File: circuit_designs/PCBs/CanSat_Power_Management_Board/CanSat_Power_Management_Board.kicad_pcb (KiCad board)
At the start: 4 copper layers, 95 x 95 mm, 62 parts, among them J1 MCU Switch (7.4V), J2 7.4V Battery, J3 Sensor Board, J4 Booster Switch (3.7V), J5 3.7V Battery, Q1 BS170, Q2 BSS84, U1 LM2596T-ADJ, U3 NE555P

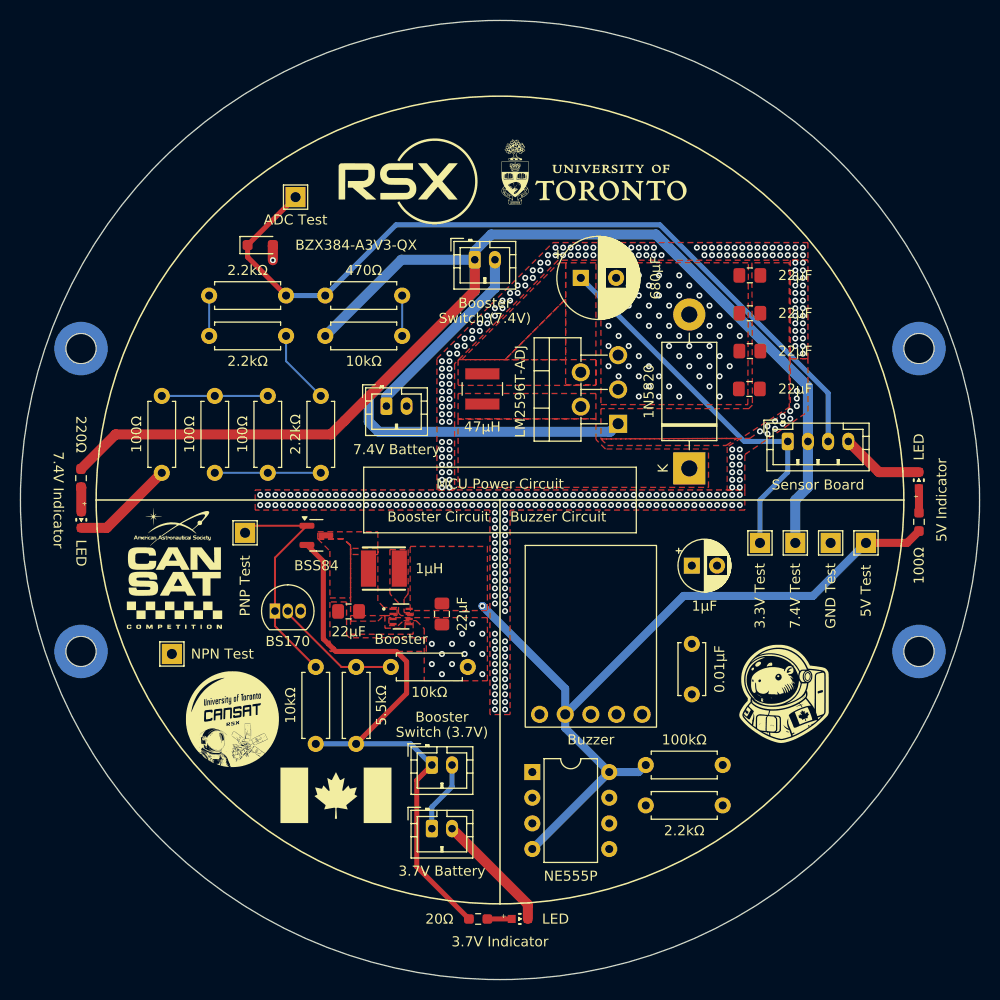
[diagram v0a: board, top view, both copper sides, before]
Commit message: fixed stiching vias - added new logo - fixed some other vias with kc
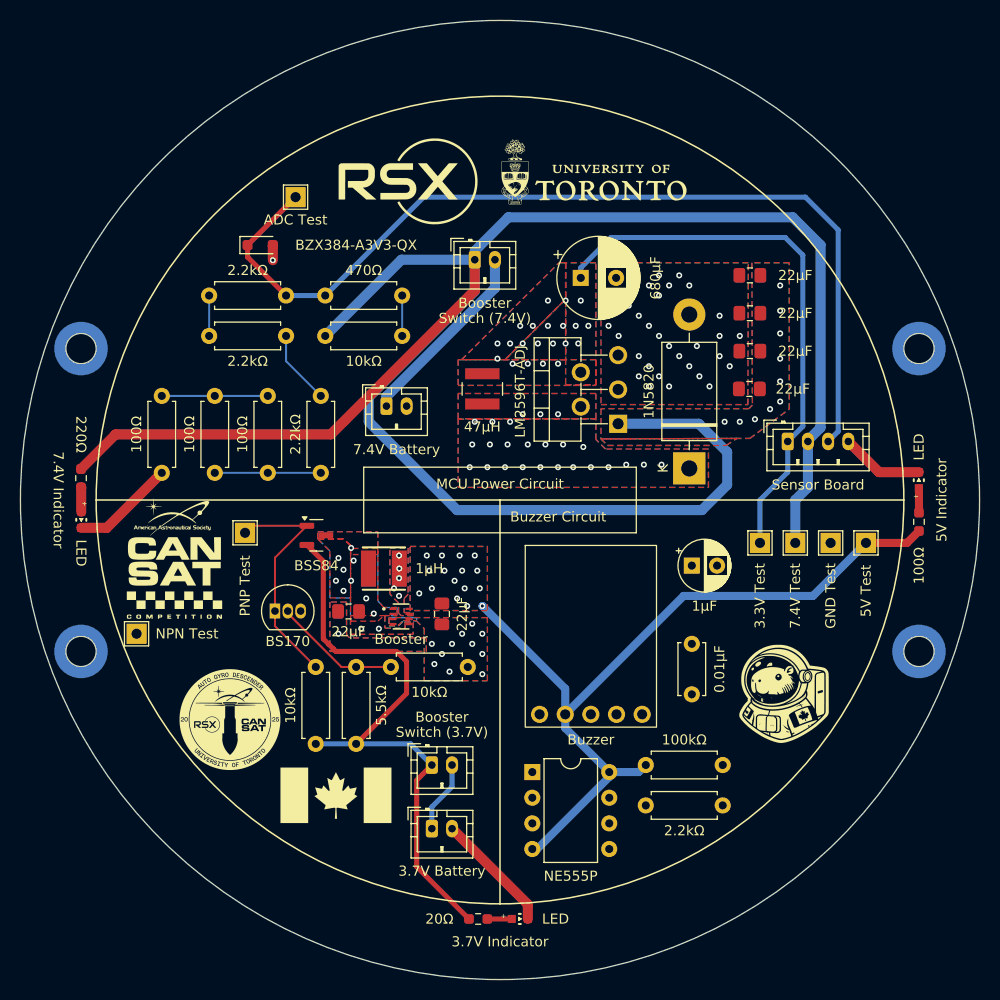
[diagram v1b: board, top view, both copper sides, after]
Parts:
- removed the G*** at (123.5, 121.8)
- added G***: LOGO, Graphics:logo, F.Cu at (123.2, 121.8)
- added G***: LOGO, Graphics:logo_x2, B.Cu at (120.8, 123.0)
- moved TP5 4.03 mm to (114.0, 113.2)
- moved G*** 1.00 mm to (117.8, 105.8)
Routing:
- net 7.4V: track 170.0 -> 211.3 mm, vias 0 -> 10
- net 3.3V: track 38.4 -> 55.2 mm, vias 0 -> 21
- net ADC: track 81.6 -> 94.7 mm
- net /5V: track 78.9 -> 79.2 mm, vias 1 -> 16
- net GND: vias 413 -> 42
- net /VIN: vias 0 -> 11
- net /SW: vias 0 -> 5
- net /OUT: vias 0 -> 25
- added copper zone on B.Cu, net /5V
- added copper zone on B.Cu, net /OUT
- added copper zone on B.Cu, net /SW
- added copper zone on B.Cu, net /VIN
- added copper zone on B.Cu, net 3.3V
- added copper zone on B.Cu, net 7.4V
- added copper zone on B.Cu, net GND
- added copper zone on In2.Cu, net GND
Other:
- board text removed: "Booster Circuit"

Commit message: fixed errors and exposed copper for thermal pads
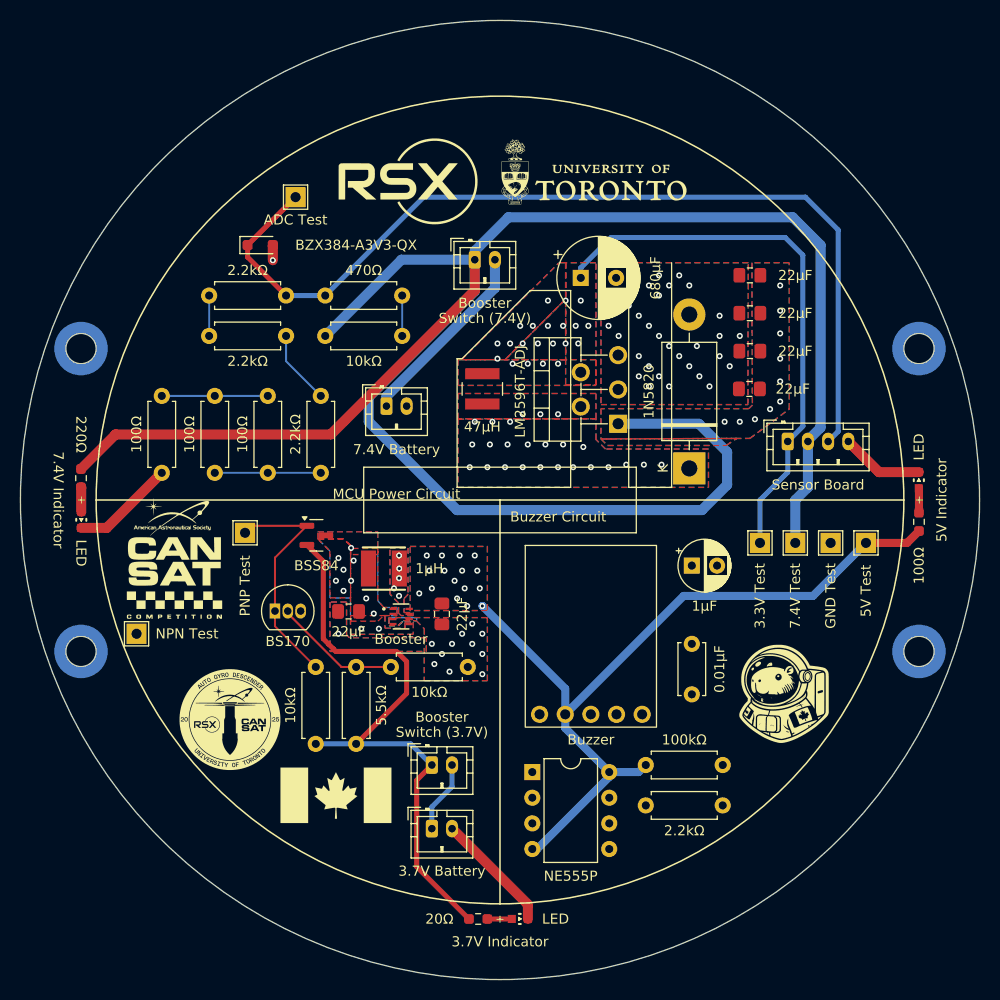
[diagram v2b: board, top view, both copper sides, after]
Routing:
- net Net-(Q1-G): track 26.7 -> 30.2 mm
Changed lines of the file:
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@@
 			(plotinvisibletext no)
 			(sketchpadsonfab no)
-			(subtractmaskfromsilk no)
+			(subtractmaskfromsilk yes)
 			(outputformat 1)
 			(mirror no)
@@
 		)
 		(fp_text user "+"
-			(at 1.6 0.3 90)
+			(at 1.9625 -0.025 90)
 			(layer "F.SilkS")
 			(effects
 				(font
-					(size 0.48 0.48)
+					(size 0.8 0.8)
 					(thickness 0.15)
 				)
@@
 		)
 		(fp_text user "+"
-			(at 1.6 0.3 0)
+			(at 1.9625 -0.005 0)
 			(layer "F.SilkS")
 			(effects
 				(font
-					(size 0.48 0.48)
+					(size 0.8 0.8)
 					(thickness 0.15)
 				)
@@
 		)
 		(fp_text user "+"
-			(at 1.6 0.3 90)
+			(at 1.9625 -0.015 90)
 			(layer "F.SilkS")
 			(effects
 				(font
-					(size 0.48 0.48)
+					(size 0.8 0.8)
 					(thickness 0.15)
 				)
@@
 			(effects
 				(font
-					(size 0.48 0.48)
+					(size 0.8 0.8)
 					(thickness 0.15)
 				)
@@
 	)
 	(gr_line
+		(start 146.25 86)
+		(end 153 79.25)
+		(stroke
+			(width 0.1)
+			(type default)
+		)
+		(layer "F.SilkS")
+	)
+	(gr_line
 		(start 136.5 103.25)
 		(end 150 103.25)
@@
 	)
 	(gr_line
+		(start 157 98.75)
+		(end 145.75 98.75)
+		(stroke
+			(width 0.1)
+			(type default)
+		)
+		(layer "F.SilkS")
+	)
+	(gr_line
 		(start 136.5 100)
 		(end 136.5 103.25)
@@
 	)
 	(gr_line
+		(start 153 79.25)
+		(end 157 79.25)
+		(stroke
+			(width 0.1)
+			(type default)
+		)
+		(layer "F.SilkS")
+	)
+	(gr_line
 		(start 150 103.25)
 		(end 163.5 103.25)
@@
 	)
 	(gr_line
+		(start 145.75 98.75)
+		(end 145.75 86)
+		(stroke
+			(width 0.1)
+			(type default)
+		)
+		(layer "F.SilkS")
+	)
+	(gr_line
 		(start 163.5 100)
 		(end 163.5 96.75)
@@
 	)
 	(gr_line
+		(start 162.75 76.5)
+		(end 162.75 98.75)
+		(stroke
+			(width 0.1)
+			(type default)
+		)
+		(layer "F.SilkS")
+	)
+	(gr_line
 		(start 136.5 96.75)
 		(end 136.5 100)
@@
 	)
 	(gr_line
+		(start 145.75 86)
+		(end 146.25 86)
+		(stroke
+			(width 0.1)
+			(type default)
+		)
+		(layer "F.SilkS")
+	)
+	(gr_line
+		(start 167 98.75)
+		(end 167 76.5)
+		(stroke
+			(width 0.1)
+			(type default)
+		)
+		(layer "F.SilkS")
+	)
+	(gr_line
+		(start 157 79.25)
+		(end 157 98.75)
+		(stroke
+			(width 0.1)
+			(type default)
+		)
+		(layer "F.SilkS")
+	)
+	(gr_line
 		(start 150 140)
 		(end 150 100)
@@
 	)
 	(gr_line
+		(start 162.75 98.75)
+		(end 167 98.75)
+		(stroke
+			(width 0.1)
+			(type default)
+		)
+		(layer "F.SilkS")
+	)
+	(gr_line
 		(start 110 100)
 		(end 190 100)
@@
 	)
 	(gr_text "NPN Test Point"
-		(at 112 112 90)
+		(at 112 111.25 90)
 		(layer "B.SilkS")
 		(effects
@@
 	)
 	(gr_text "MCU Power Circuit"
-		(at 150 99 0)
+		(at 139.75 100 0)
 		(layer "F.SilkS")
 		(effects
@@
 	)
 	(segment
-		(start 125.68 115.25)
+		(start 128.98 111.95)
+		(end 128.98 111)
+		(width 0.2)
+		(layer "In2.Cu")
+		(net 13)
+	)
+	(segment
+		(start 126.68 114.25)
 		(end 128.98 111.95)
 		(width 0.2)
@@
 	)
 	(segment
-		(start 117.5 115.25)
-		(end 125.68 115.25)
+		(start 114 113.25)
+		(end 115 114.25)
 		(width 0.2)
 		(layer "In2.Cu")
@@
 	)
 	(segment
-		(start 128.98 111.95)
-		(end 128.98 111)
+		(start 115 114.25)
+		(end 126.68 114.25)
 		(width 0.2)
 		(layer "In2.Cu")
@@
 			)
 		)
+	)
+	(zone
+		(net 0)
+		(net_name "")
+		(layer "B.Mask")
+		(hatch edge 0.5)
+		(connect_pads
+			(clearance 0)
+		)
+		(min_thickness 0.25)
+		(filled_areas_thickness no)
+		(fill yes
+			(thermal_gap 0.5)
+			(thermal_bridge_width 0.5)
+		)
+		(polygon
+			(pts
+				(xy 165.75 76.5) (xy 155.801613 76.5) (xy 146.202174 86.099439) (xy 145.850534 86.099439) (xy 145.84777 86.102203)
+				(xy 145.84777 98.743733) (xy 145.857585 98.753548) (xy 165.75 98.753548) (xy 165.75 98.753548)
+			)
+		)
+	)
+	(zone
+		(net 0)
+		(net_name "")
+		(layer "B.Mask")
+		(hatch edge 0.5)
+		(connect_pads
+			(clearance 0)
+		)
+		(min_thickness 0.25)
+		(filled_areas_thickness no)
+		(fill yes
+			(thermal_gap 0.5)
+			(thermal_bridge_width 0.5)
+		)
+		(polygon
+			(pts
+				(xy 148.770992 104.579772) (xy 139.101774 104.579772) (xy 139.101774 114.55319) (xy 148.69681 114.55319)
+				(xy 148.770992 114.479008)
+			)
+		)
